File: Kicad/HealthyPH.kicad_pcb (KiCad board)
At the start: 2 copper layers, 68.4 x 53.2 mm, 35 parts, among them CON1 LB_BarrelJack, P1 CONN_8, P2 V+_WallWart, Q1 TIP122, Q2 TIP122, U1 MCP6241, U2 MCP3901, U5 LM7805, X1 CRYSTAL

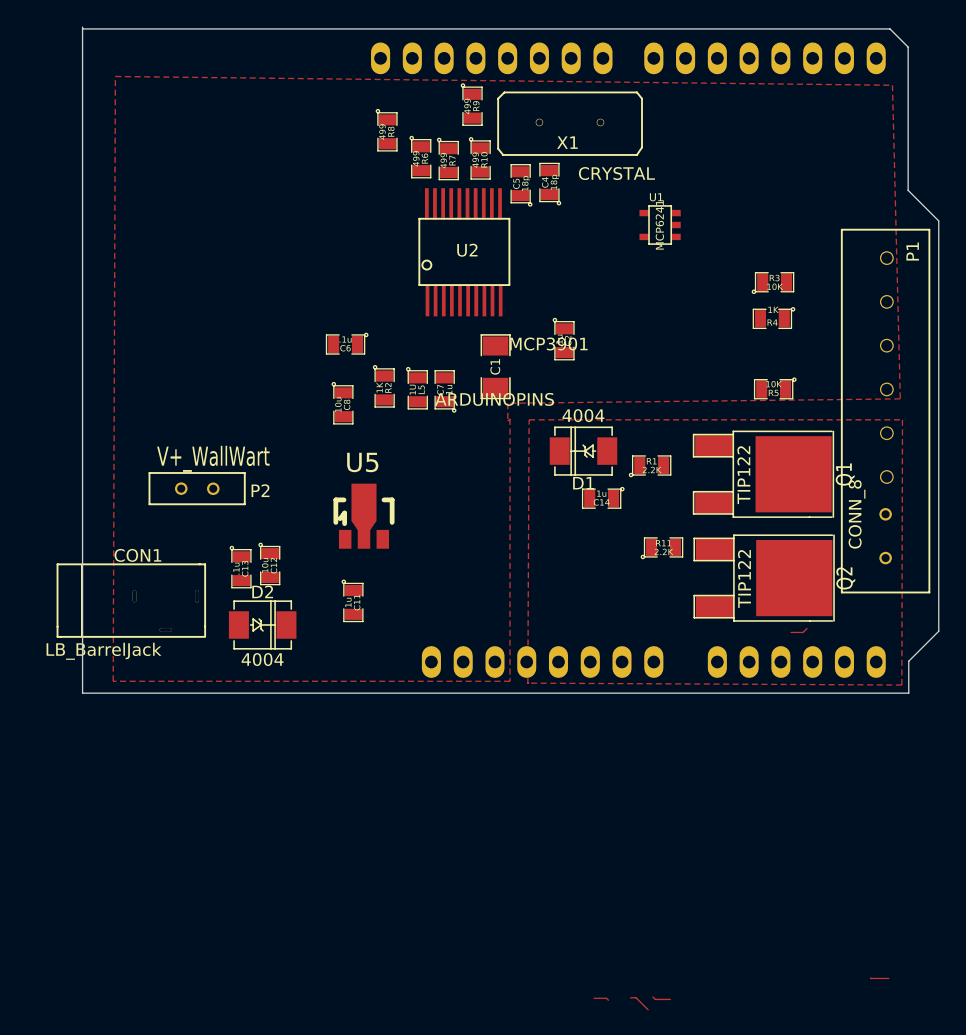
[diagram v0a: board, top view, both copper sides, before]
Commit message: Layout with traces - ran through ERC and DRC
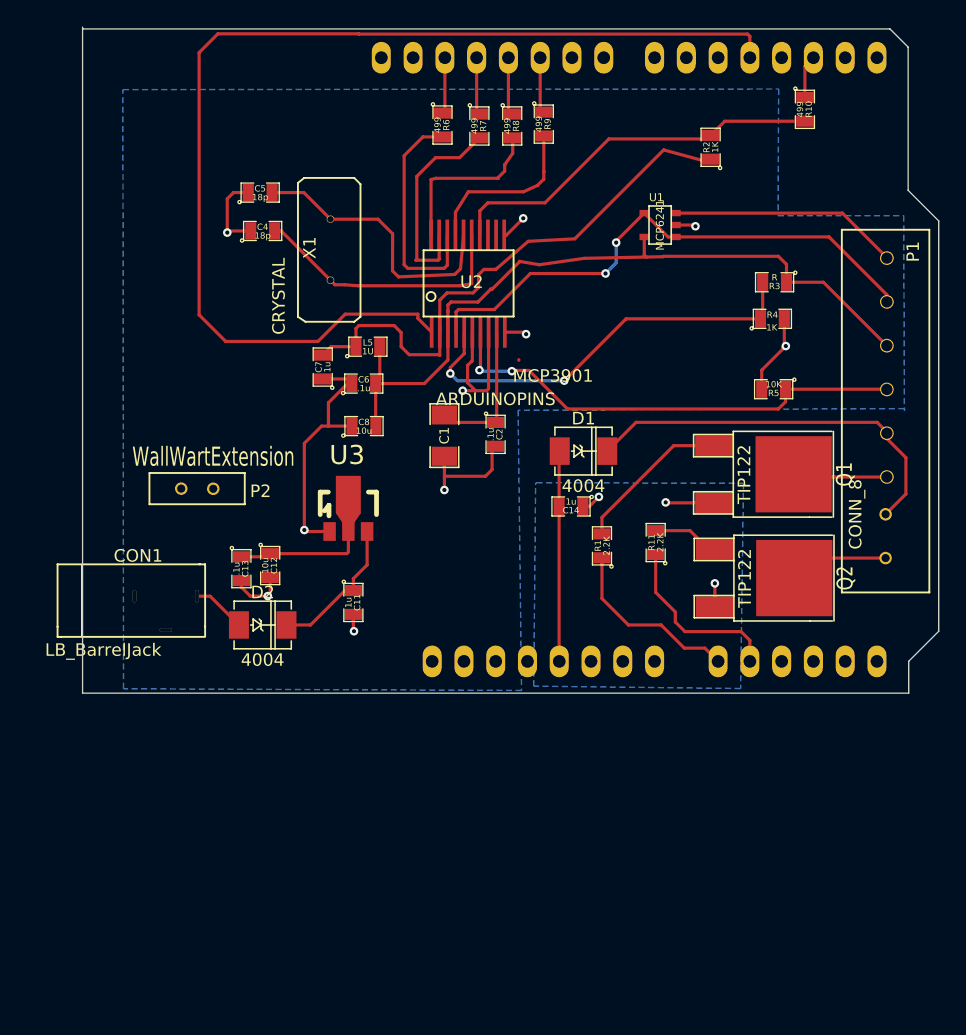
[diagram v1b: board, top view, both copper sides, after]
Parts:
- removed U5: LM7805, LB_SOT89_3
- added U3: MC78L05, LB_SOT89_3, F.Cu at (172.2, 103.4)
- P2: value V+_WallWart -> WallWartExtension
- R3: value 10K -> R
- moved R2 32.4 mm to (201.2, 74.6), turned to 90 degrees
- moved R10 26.2 mm to (208.8, 71.5)
- moved C4 23.3 mm to (165.4, 81.2), turned to 0 degrees
- moved C5 20.8 mm to (165.2, 78.2), turned to 0 degrees
- moved X1 16.1 mm to (168.2, 77.0), turned to 270 degrees
- moved R8 9.99 mm to (185.3, 72.9)
- moved C7 9.92 mm to (170.2, 92.1)
- moved C2 9.29 mm to (184.0, 97.5)
- moved R1 7.56 mm to (192.5, 106.4), turned to 90 degrees
- moved C1 6.87 mm to (179.9, 97.6)
- moved R9 5.88 mm to (187.9, 72.7)
- moved L5 5.27 mm to (173.8, 90.5), turned to 0 degrees
- moved R7 3.70 mm to (182.7, 72.9)
- moved C6 3.45 mm to (173.5, 93.5), turned to 0 degrees
- moved R6 3.19 mm to (179.8, 72.8)
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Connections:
- net /Digital Access/OSC1 renamed N-0000027
- net /Digital Access/OSC2 renamed N-0000031
- net /Digital Access/RFIN+ renamed N-0000032
- ARD1 pad 13: (no net) -> /Arduino/~DR
- ARD1 pad 15: (no net) -> /Arduino/~RESET
- ARD1 pad 21: (no net) -> /Arduino/~CS
- ARD1 pad 22: (no net) -> /Arduino/MOSI
- ARD1 pad 23: (no net) -> /Arduino/MISO
- ARD1 pad 24: (no net) -> /Arduino/SCLK
- C11 pad 1: /Wall Wart/Vin -> N-0000033
- C12 pad 1: +5V -> N-0000034
- C13 pad 1: +5V -> N-0000034
- C6 pad 1: +5V -> AGND
- C6 pad 2: N-0000034 -> /Digital Access/V+_WallWart
- C7 pad 2: +5V -> N-0000030
- C8 pad 1: N-0000034 -> AGND
- C8 pad 2: AGND -> /Digital Access/V+_WallWart
- CON1 pad 1: /Wall Wart/Vin -> N-0000036
- D1 pad 1: /Pumps/V+_DownPump -> /Arduino/V+_ARD
- D1 pad 2: /Arduino/V+_ARD -> /Pumps/V+_DownPump
- D2 pad 1: /Wall Wart/Vin -> N-0000036
- D2 pad 2: /Wall Wart/Vin -> N-0000033
- L5 pad 1: +5V -> N-0000030
- L5 pad 2: +5V -> /Digital Access/V+_WallWart
- P1 pad 3: +5V -> /Digital Access/V+_WallWart
- P2 pad 1: +5V -> AGND
- P2 pad 2: +5V -> (no net)
- Q2 pad 1: /Pumps/PUMP -> N-0000026
- R10 pad 1: (no net) -> /Arduino/~DR
- R10 pad 2: +5V -> /Digital Access/~DR
- R11 pad 2: /Pumps/PUMP -> N-0000026
- R2 pad 1: +5V -> N-0000030
- R2 pad 2: +5V -> /Digital Access/~DR
- R3 pad 1: /pH/V+_WallWart -> /Digital Access/V+_WallWart
- R3 pad 2: /Digital Access/pH_ADC+ -> /Digital Access/pH_ADC-
- R4 pad 1: /Digital Access/pH_ADC+ -> /Digital Access/pH_ADC-
- R6 pad 1: (no net) -> /Arduino/SCLK
- R7 pad 1: (no net) -> /Arduino/MISO
- R8 pad 1: (no net) -> /Arduino/MOSI
- R9 pad 1: (no net) -> /Arduino/~CS
- U1 pad 5: /pH/V+_WallWart -> /Digital Access/V+_WallWart
- U2 pad 1: (no net) -> /Arduino/~RESET
- U2 pad 10: (no net) -> AGND
- U2 pad 14: +5V -> /Digital Access/~DR
- U2 pad 2: +5V -> N-0000030
- U2 pad 3: +5V -> /Digital Access/V+_WallWart
- U2 pad 5: /Digital Access/pH_ADC+ -> /Digital Access/pH_ADC-
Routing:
- net /Arduino/~RESET: track 0.00 -> 88.6 mm
- net AGND: track 0.00 -> 65.8 mm, vias 0 -> 10
- net /Digital Access/V+_WallWart: track 0.00 -> 59.7 mm
- net N-0000030: track 0.00 -> 45.0 mm
- net /Digital Access/pH_ADC+: track 0.00 -> 44.0 mm, vias 0 -> 2
- net /Temperature/Temp: track 0.00 -> 38.2 mm, vias 0 -> 2
- net /Digital Access/pH_ADC-: track 0.00 -> 34.1 mm, vias 0 -> 2
- net /Pumps/V+_DownPump: track 0.00 -> 31.5 mm
- net /Digital Access/~DR: track 0.00 -> 30.9 mm
- net N-0000031: track 0.00 -> 22.5 mm
- net N-0000027: track 0.00 -> 21.4 mm
- net /Digital Access/SCLK_ISO: track 0.00 -> 18.5 mm
- net /pH/pH_V+(in): track 0.00 -> 18.4 mm
- net /Arduino/V+_ARD: track 0.00 -> 16.8 mm
- net /Digital Access/MISO_ISO: track 0.00 -> 16.8 mm
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- added copper zone on B.Cu, net AGND
- added copper zone on B.Cu, net GND
- removed copper zone on F.Cu, net AGND
- removed copper zone on F.Cu, net GND
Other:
- net class Default: clearance 0.006 -> 0.254; trace_width 0.006 -> 0.254; via_dia 0.01062 -> 0.6858; via_drill 0.005118 -> 0.3302
- net class POWER removed
- rule trace_clearance: 0.006 -> 0.254
- rule trace_min: 0.006 -> 0.254
- rule via_min_drill: 0.005 -> 0.3302
- rule via_min_size: 0.001 -> 0.6858

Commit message: updates to layout based on DRC/DFM checks
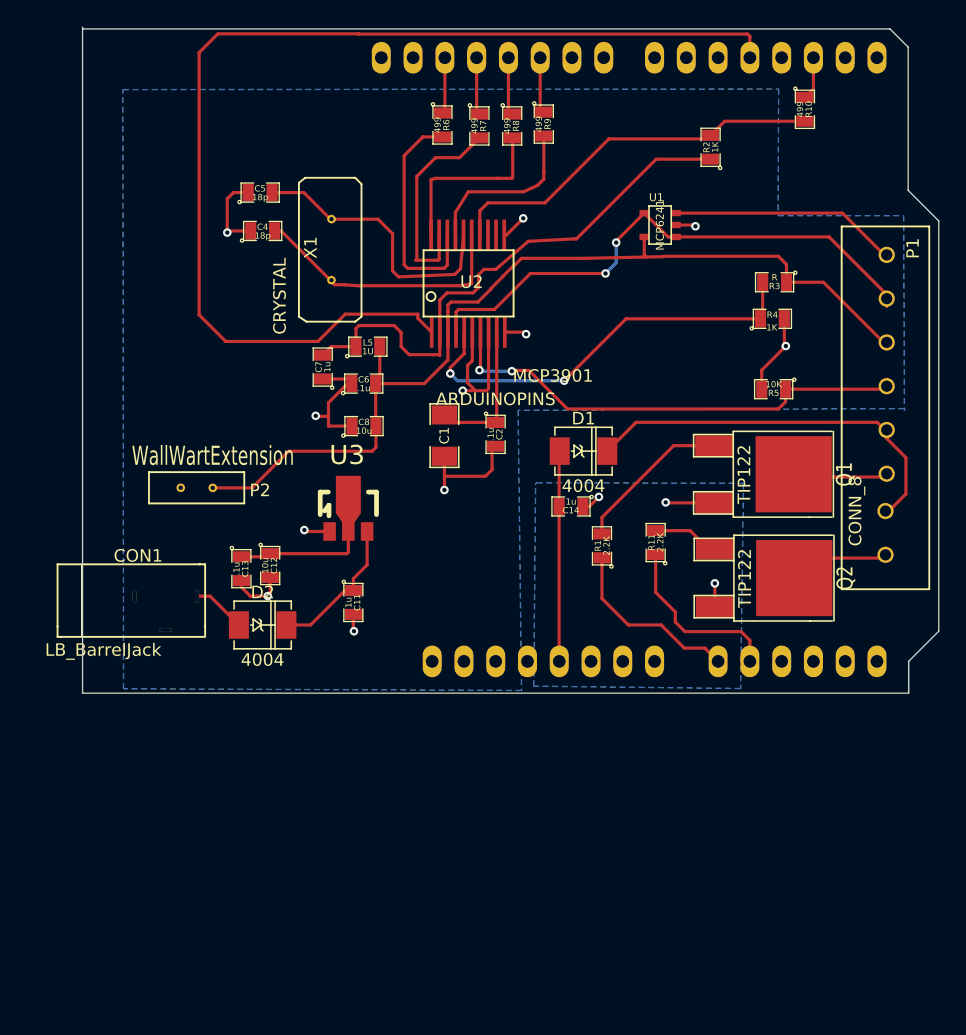
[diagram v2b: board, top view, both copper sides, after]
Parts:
- moved P1 0.26 mm to (218.7, 80.9)
- moved X1 0.08 mm to (168.3, 77.0)
- moved P2 0.08 mm to (156.3, 103.0)
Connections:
- P2 pad 2: (no net) -> /Digital Access/V+_WallWart
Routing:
- net /Digital Access/V+_WallWart: track 59.7 -> 75.8 mm
- net AGND: track 65.8 -> 57.4 mm, vias 10 -> 11
- net /Digital Access/MOSI_ISO: track 13.6 -> 14.3 mm
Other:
- net class Default: via_drill 0.3302 -> 0.34
- rule via_min_drill: 0.3302 -> 0.34

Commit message: Updated layout - no DRC or DFM issues
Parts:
- R3: value R -> 10K
- moved P1 0.19 mm to (218.7, 81.1)
- moved X1 0.11 mm to (168.4, 77.0)
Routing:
- net AGND: track 57.4 -> 61.0 mm
- net /Arduino/~RESET: track 88.6 -> 85.4 mm, vias 0 -> 1
- net /Digital Access/~DR: track 30.9 -> 32.7 mm
- net /Digital Access/V+_WallWart: track 75.8 -> 77.2 mm
- net /Digital Access/MISO_ISO: track 16.8 -> 18.1 mm
- net /Pumps/DownPump: track 15.2 -> 14.6 mm
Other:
- board size 68.4 x 53.2 mm -> 68.6 x 53.4 mm
- net class Default: via_drill 0.34 -> 0.3302
- net class Power added: clearance 0.254, trace_width 0.6096, via_dia 0.889, via_drill 0.4318
- rule via_min_drill: 0.34 -> 0.3302
